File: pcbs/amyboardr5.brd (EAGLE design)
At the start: 106.1 x 47.5 mm, 146 parts, among them Q2 S8050, Q5 S8050, U1 PCM9211PT, U15 H11L1SR2M, U16 SPX3819, U2 ESP32­S2­SOLO, U3 SPX3819, U4 TL074CD, U6 HX3608, Y1 22.5792MHZ

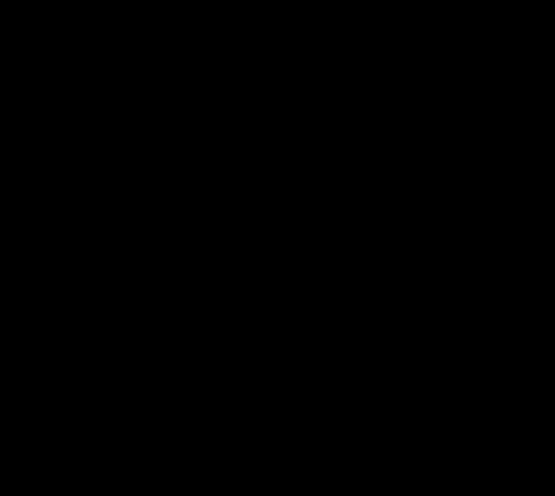
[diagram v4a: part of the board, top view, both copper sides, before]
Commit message: Added ferrite beads in Pi circuits to + and -12v lines.
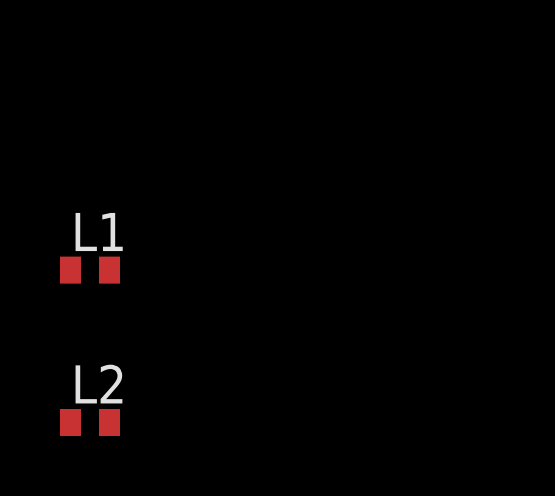
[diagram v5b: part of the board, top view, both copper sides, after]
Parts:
- added L1, L2: BLM15HB121SN1, inductors:0402
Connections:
- new net N$16: C31.2, D10.A, L2.1
- new net N$24: C27.1, D8.C, L1.1
- new net N$25: C29.1
- new net N$30: R18.2
- net -12V: now also L2.2; no longer C31.2, D10.A
- net 12V: now also L1.2; no longer C27.1, C29.1, D8.C, R18.2
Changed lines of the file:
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@@
 <attribute name="VALUE" x="36.83" y="46.99" size="1.27" layer="27" rot="R90"/>
+</element>
+<element name="L1" library="inductors" library_urn="urn:adsk.eagle:library:243" package="0402" package3d_urn="urn:adsk.eagle:package:15132/1" value="BLM15HB121SN1" x="-284.226" y="-1072.388" smashed="yes">
+<attribute name="NAME" x="-284.861" y="-1071.753" size="1.27" layer="25"/>
+<attribute name="POPULARITY" value="0" x="-284.226" y="-1072.388" size="1.778" layer="27" display="off"/>
+<attribute name="VALUE" x="-284.861" y="-1074.293" size="1.27" layer="27"/>
+</element>
+<element name="L2" library="inductors" library_urn="urn:adsk.eagle:library:243" package="0402" package3d_urn="urn:adsk.eagle:package:15132/1" value="BLM15HB121SN1" x="-284.226" y="-1077.468" smashed="yes">
+<attribute name="NAME" x="-284.861" y="-1076.833" size="1.27" layer="25"/>
+<attribute name="POPULARITY" value="0" x="-284.226" y="-1077.468" size="1.778" layer="27" display="off"/>
+<attribute name="VALUE" x="-284.861" y="-1079.373" size="1.27" layer="27"/>
 </element>
 </elements>
@@
 <contactref element="R19" pad="1"/>
 <contactref element="C28" pad="2"/>
-<contactref element="C27" pad="2"/>
 <contactref element="D9" pad="C"/>
 <contactref element="C31" pad="1"/>
@@
 <contactref element="C9" pad="2"/>
 <contactref element="R21" pad="2"/>
+<contactref element="C27" pad="2"/>
 <wire x1="93.69" y1="45.582" x2="95.62" y2="43.652" width="0" layer="19" extent="1-1"/>
 <wire x1="95.62" y1="39.652" x2="95.62" y2="43.652" width="0" layer="19" extent="1-1"/>
@@
 <wire x1="41.148" y1="33.02" x2="36.83" y2="33.02" width="0" layer="19" extent="1-1"/>
 <wire x1="41.656" y1="34.036" x2="41.148" y2="33.02" width="0" layer="19" extent="1-1"/>
+<wire x1="42.418" y1="36.950334375" x2="41.656" y2="34.036" width="0" layer="19" extent="1-1"/>
 <wire x1="53.086" y1="36.950334375" x2="52.782" y2="31.588" width="0" layer="19" extent="1-1"/>
 <wire x1="28.006" y1="14.732" x2="28.448" y2="21.59" width="0" layer="19" extent="1-1"/>
@@
 <wire x1="17.206" y1="2.76" x2="19.606" y2="10.26" width="0" layer="19" extent="1-1"/>
 <wire x1="11.21" y1="3.236" x2="17.206" y2="2.76" width="0" layer="19" extent="1-16"/>
-<wire x1="42.418" y1="36.950334375" x2="37.084" y2="36.83" width="0" layer="19" extent="1-1"/>
 <wire x1="46.331" y1="45.72" x2="42.418" y2="36.950334375" width="0" layer="19" extent="1-1"/>
 <wire x1="45.706" y1="47.27" x2="46.331" y2="45.72" width="0" layer="19" extent="1-1"/>
 <wire x1="50.306" y1="47.27" x2="46.331" y2="45.72" width="0" layer="19" extent="1-1"/>
-<wire x1="34.544" y1="48.752" x2="42.418" y2="36.950334375" width="0" layer="19" extent="1-1"/>
 <wire x1="59.93" y1="47.308" x2="50.306" y2="47.27" width="0" layer="19" extent="1-1"/>
 <wire x1="60.555" y1="45.758" x2="59.93" y2="47.308" width="0" layer="19" extent="1-1"/>
@@
 <wire x1="83.934" y1="42.852" x2="93.69" y2="45.582" width="0" layer="19" extent="1-1"/>
 <wire x1="73.684" y1="35.132" x2="66.434" y2="42.852" width="0" layer="19" extent="1-1"/>
+<wire x1="34.544" y1="48.752" x2="45.706" y2="47.27" width="0" layer="19" extent="1-1"/>
 </signal>
 <signal name="3.3V">
@@
 </signal>
 <signal name="-12V">
-<contactref element="D10" pad="A"/>
-<contactref element="C31" pad="2"/>
 <contactref element="C20" pad="2"/>
 <contactref element="U4" pad="11"/>
 <contactref element="C21" pad="2"/>
-<wire x1="6.858" y1="33.528" x2="3.556" y2="33.528" width="0" layer="19" extent="1-1"/>
-<wire x1="10.16" y1="33.528" x2="6.858" y2="33.528" width="0" layer="19" extent="1-1"/>
-<wire x1="17.519" y1="34.29" x2="10.16" y2="33.528" width="0" layer="19" extent="1-1"/>
-<wire x1="57.593" y1="15.24" x2="17.519" y2="34.29" width="0" layer="19" extent="1-1"/>
+<contactref element="L2" pad="2"/>
+<wire x1="57.593" y1="15.24" x2="-283.576" y2="-1077.468" width="0" layer="19" extent="1-1"/>
+<wire x1="6.858" y1="33.528" x2="57.593" y2="15.24" width="0" layer="19" extent="1-1"/>
+<wire x1="3.556" y1="33.528" x2="6.858" y2="33.528" width="0" layer="19" extent="1-1"/>
 </signal>
 <signal name="+12V">
@@
 </signal>
 <signal name="12V">
-<contactref element="C28" pad="1"/>
-<contactref element="C27" pad="1"/>
-<contactref element="D8" pad="C"/>
-<contactref element="C29" pad="1"/>
 <contactref element="R17" pad="2"/>
-<contactref element="R18" pad="2"/>
 <contactref element="C32" pad="1"/>
 <contactref element="U3" pad="1"/>
 <contactref element="U3" pad="3"/>
-<wire x1="33.274" y1="38.1" x2="36.576" y2="38.1" width="0" layer="19" extent="1-1"/>
-<wire x1="29.972" y1="38.1" x2="33.274" y2="38.1" width="0" layer="19" extent="1-1"/>
-<wire x1="35.56" y1="34.036" x2="36.576" y2="38.1" width="0" layer="19" extent="1-1"/>
-<wire x1="39.37" y1="34.036" x2="35.56" y2="34.036" width="0" layer="19" extent="1-1"/>
+<contactref element="C28" pad="1"/>
+<contactref element="L1" pad="2"/>
+<wire x1="35.56" y1="34.036" x2="-283.576" y2="-1072.388" width="0" layer="19" extent="1-1"/>
 <wire x1="35.306" y1="27.94" x2="35.56" y2="34.036" width="0" layer="19" extent="1-1"/>
+<wire x1="29.972" y1="38.1" x2="35.56" y2="34.036" width="0" layer="19" extent="1-1"/>
 <wire x1="36.134" y1="21.0519" x2="35.306" y2="27.94" width="0" layer="19" extent="1-1"/>
 <wire x1="38.034" y1="21.0519" x2="36.134" y2="21.0519" width="0" layer="19" extent="1-1"/>
-<wire x1="38.107" y1="20.574" x2="38.034" y2="21.0519" width="0" layer="19" extent="1-1"/>
 </signal>
 <signal name="N$29">
@@
 <wire x1="34.544" y1="36.592" x2="46.908046875" y2="40.64" width="0" layer="19" extent="1-1"/>
 </signal>
+<signal name="N$16">
+<contactref element="D10" pad="A"/>
+<contactref element="C31" pad="2"/>
+<contactref element="L2" pad="1"/>
+<wire x1="17.519" y1="34.29" x2="-284.876" y2="-1077.468" width="0" layer="19" extent="1-1"/>
+<wire x1="10.16" y1="33.528" x2="17.519" y2="34.29" width="0" layer="19" extent="1-1"/>
+</signal>
+<signal name="N$24">
+<contactref element="C27" pad="1"/>
+<contactref element="L1" pad="1"/>
+<contactref element="D8" pad="C"/>
+<wire x1="33.274" y1="38.1" x2="-284.876" y2="-1072.388" width="0" layer="19" extent="1-1"/>
+<wire x1="38.107" y1="20.574" x2="33.274" y2="38.1" width="0" layer="19" extent="1-1"/>
+</signal>
+<signal name="N$25">
+<contactref element="C29" pad="1"/>
+</signal>
+<signal name="N$30">
+<contactref element="R18" pad="2"/>
+</signal>
 </signals>

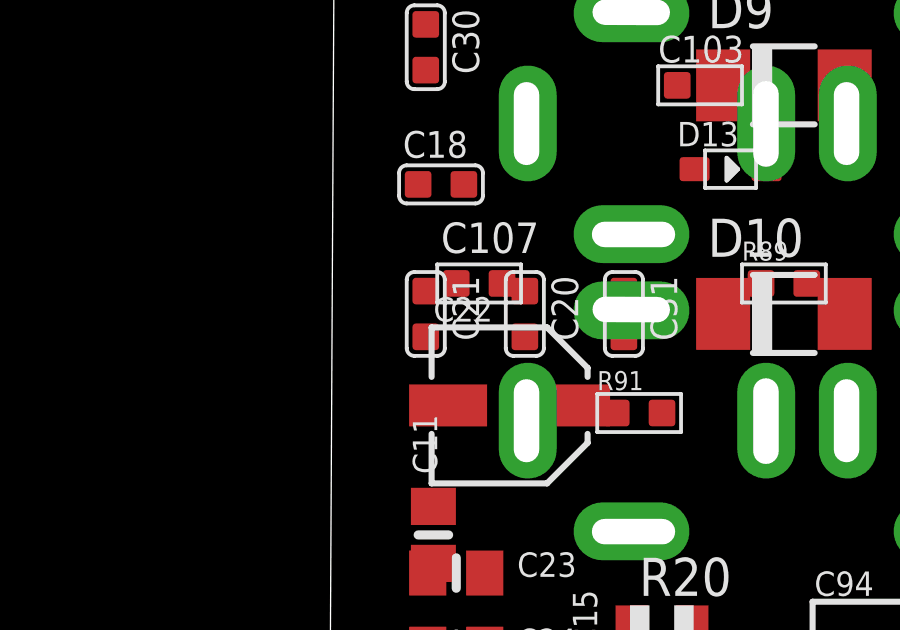
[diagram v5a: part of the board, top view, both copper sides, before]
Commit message: Moved GP8413 and 5V LDO to +12V_UNFILTERED.
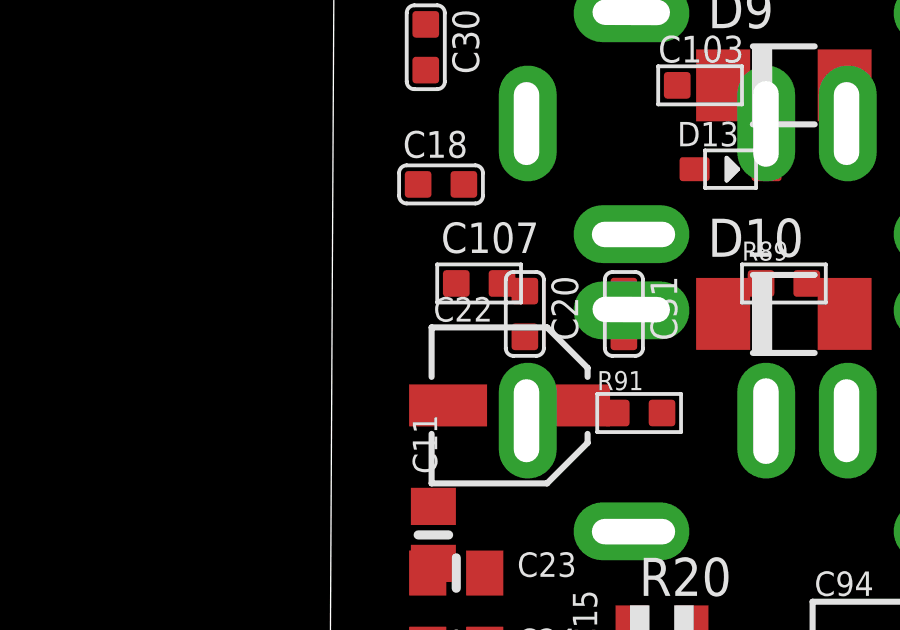
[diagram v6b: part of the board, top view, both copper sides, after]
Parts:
- removed C21: 20pF, Discrete-new:C0603
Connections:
- removed net N$24: C27.1, D8.C, L1.1
- new net 12V_UNFILTERED: C26.1, C27.1, C32.1, D8.C, L1.1, U$7.5, U3.1, U3.3
- net +12V: no longer C21.1, C26.1, U$7.5
- net -12V: no longer C21.2
- net 12V: no longer C32.1, U3.1, U3.3
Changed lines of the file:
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@@
 <attribute name="VALUE" x="6.9215" y="34.29" size="0.635" layer="27" ratio="10" rot="R270" align="center"/>
-</element>
-<element name="C21" library="Discrete-new" package="C0603" value="20pF" x="3.556" y="34.29" smashed="yes">
-<attribute name="NAME" x="4.445" y="35.56" size="0.889" layer="25" ratio="11" rot="R270"/>
-<attribute name="NAME" x="3.302" y="35.56" size="0.635" layer="33" ratio="10" rot="R270"/>
-<attribute name="VALUE" x="3.6195" y="34.29" size="0.635" layer="27" ratio="10" rot="R270" align="center"/>
 </element>
 <element name="R20" library="adafruit" package="R0805" value="10K" x="11.43" y="23.876" smashed="yes">
@@
 <contactref element="C20" pad="2"/>
 <contactref element="U4" pad="11"/>
-<contactref element="C21" pad="2"/>
 <contactref element="L2" pad="2"/>
 <wire x1="57.593" y1="15.24" x2="-283.576" y2="-1077.468" width="0" layer="19" extent="1-1"/>
 <wire x1="6.858" y1="33.528" x2="57.593" y2="15.24" width="0" layer="19" extent="1-1"/>
-<wire x1="3.556" y1="33.528" x2="6.858" y2="33.528" width="0" layer="19" extent="1-1"/>
 </signal>
 <signal name="+12V">
 <contactref element="U4" pad="4"/>
-<contactref element="C21" pad="1"/>
-<contactref element="U$7" pad="5"/>
-<contactref element="C26" pad="1"/>
-<wire x1="3.556" y1="35.052" x2="3.622" y2="20.574" width="0" layer="19" extent="1-1"/>
-<wire x1="52.643" y1="15.24" x2="3.556" y2="35.052" width="0" layer="19" extent="1-1"/>
-<wire x1="51.054" y1="24.07" x2="52.643" y2="15.24" width="0" layer="19" extent="1-1"/>
 </signal>
 <signal name="GND3">
@@
 <signal name="12V">
 <contactref element="R17" pad="2"/>
-<contactref element="C32" pad="1"/>
-<contactref element="U3" pad="1"/>
-<contactref element="U3" pad="3"/>
 <contactref element="C28" pad="1"/>
 <contactref element="L1" pad="2"/>
 <wire x1="35.56" y1="34.036" x2="-283.576" y2="-1072.388" width="0" layer="19" extent="1-1"/>
-<wire x1="35.306" y1="27.94" x2="35.56" y2="34.036" width="0" layer="19" extent="1-1"/>
 <wire x1="29.972" y1="38.1" x2="35.56" y2="34.036" width="0" layer="19" extent="1-1"/>
-<wire x1="36.134" y1="21.0519" x2="35.306" y2="27.94" width="0" layer="19" extent="1-1"/>
-<wire x1="38.034" y1="21.0519" x2="36.134" y2="21.0519" width="0" layer="19" extent="1-1"/>
 </signal>
 <signal name="N$29">
@@
 <wire x1="10.16" y1="33.528" x2="17.519" y2="34.29" width="0" layer="19" extent="1-1"/>
 </signal>
-<signal name="N$24">
+<signal name="12V_UNFILTERED">
 <contactref element="C27" pad="1"/>
 <contactref element="L1" pad="1"/>
 <contactref element="D8" pad="C"/>
-<wire x1="33.274" y1="38.1" x2="-284.876" y2="-1072.388" width="0" layer="19" extent="1-1"/>
-<wire x1="38.107" y1="20.574" x2="33.274" y2="38.1" width="0" layer="19" extent="1-1"/>
+<contactref element="U3" pad="1"/>
+<contactref element="C32" pad="1"/>
+<contactref element="U3" pad="3"/>
+<contactref element="U$7" pad="5"/>
+<contactref element="C26" pad="1"/>
+<wire x1="51.054" y1="24.07" x2="-284.876" y2="-1072.388" width="0" layer="19" extent="1-1"/>
+<wire x1="38.034" y1="21.0519" x2="51.054" y2="24.07" width="0" layer="19" extent="1-1"/>
+<wire x1="38.107" y1="20.574" x2="38.034" y2="21.0519" width="0" layer="19" extent="1-1"/>
+<wire x1="36.134" y1="21.0519" x2="38.034" y2="21.0519" width="0" layer="19" extent="1-1"/>
+<wire x1="35.306" y1="27.94" x2="36.134" y2="21.0519" width="0" layer="19" extent="1-1"/>
+<wire x1="33.274" y1="38.1" x2="35.306" y2="27.94" width="0" layer="19" extent="1-1"/>
+<wire x1="3.622" y1="20.574" x2="36.134" y2="21.0519" width="0" layer="19" extent="1-1"/>
 </signal>
 <signal name="N$25">

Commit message: copying usb fb
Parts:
- removed L1, L2: BLM15HB121SN1, inductors:0402
- added FB1, FB2: 100Mhz@120R, rcl:R0805
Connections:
- net -12V: now also FB1.2; no longer L2.2
- net 12V: now also FB2.2; no longer L1.2
- net 12V_UNFILTERED: now also FB2.1; no longer L1.1
- net N$16: now also FB1.1; no longer L2.1
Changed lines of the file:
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@@
 <attribute name="VALUE" x="36.83" y="46.99" size="1.27" layer="27" rot="R90"/>
 </element>
-<element name="L1" library="inductors" library_urn="urn:adsk.eagle:library:243" package="0402" package3d_urn="urn:adsk.eagle:package:15132/1" value="BLM15HB121SN1" x="-284.226" y="-1072.388" smashed="yes">
-<attribute name="NAME" x="-284.861" y="-1071.753" size="1.27" layer="25"/>
-<attribute name="POPULARITY" value="0" x="-284.226" y="-1072.388" size="1.778" layer="27" display="off"/>
-<attribute name="VALUE" x="-284.861" y="-1074.293" size="1.27" layer="27"/>
+<element name="FB1" library="rcl" package="R0805" value="100Mhz@120R" x="-283.718" y="-1083.056" smashed="yes">
+<attribute name="NAME" x="-284.353" y="-1081.786" size="1.27" layer="25"/>
+<attribute name="VALUE" x="-284.353" y="-1085.596" size="1.27" layer="27"/>
 </element>
-<element name="L2" library="inductors" library_urn="urn:adsk.eagle:library:243" package="0402" package3d_urn="urn:adsk.eagle:package:15132/1" value="BLM15HB121SN1" x="-284.226" y="-1077.468" smashed="yes">
-<attribute name="NAME" x="-284.861" y="-1076.833" size="1.27" layer="25"/>
-<attribute name="POPULARITY" value="0" x="-284.226" y="-1077.468" size="1.778" layer="27" display="off"/>
-<attribute name="VALUE" x="-284.861" y="-1079.373" size="1.27" layer="27"/>
+<element name="FB2" library="rcl" package="R0805" value="100Mhz@120R" x="-283.718" y="-1089.406" smashed="yes">
+<attribute name="NAME" x="-284.353" y="-1088.136" size="1.27" layer="25"/>
+<attribute name="VALUE" x="-284.353" y="-1091.946" size="1.27" layer="27"/>
 </element>
 </elements>
@@
 <contactref element="C20" pad="2"/>
 <contactref element="U4" pad="11"/>
-<contactref element="L2" pad="2"/>
-<wire x1="57.593" y1="15.24" x2="-283.576" y2="-1077.468" width="0" layer="19" extent="1-1"/>
+<contactref element="FB1" pad="2"/>
+<wire x1="57.593" y1="15.24" x2="-282.768" y2="-1083.056" width="0" layer="19" extent="1-1"/>
 <wire x1="6.858" y1="33.528" x2="57.593" y2="15.24" width="0" layer="19" extent="1-1"/>
 </signal>
@@
 <contactref element="R17" pad="2"/>
 <contactref element="C28" pad="1"/>
-<contactref element="L1" pad="2"/>
-<wire x1="35.56" y1="34.036" x2="-283.576" y2="-1072.388" width="0" layer="19" extent="1-1"/>
+<contactref element="FB2" pad="2"/>
+<wire x1="35.56" y1="34.036" x2="-282.768" y2="-1089.406" width="0" layer="19" extent="1-1"/>
 <wire x1="29.972" y1="38.1" x2="35.56" y2="34.036" width="0" layer="19" extent="1-1"/>
 </signal>
@@
 <contactref element="D10" pad="A"/>
 <contactref element="C31" pad="2"/>
-<contactref element="L2" pad="1"/>
-<wire x1="17.519" y1="34.29" x2="-284.876" y2="-1077.468" width="0" layer="19" extent="1-1"/>
+<contactref element="FB1" pad="1"/>
+<wire x1="17.519" y1="34.29" x2="-284.668" y2="-1083.056" width="0" layer="19" extent="1-1"/>
 <wire x1="10.16" y1="33.528" x2="17.519" y2="34.29" width="0" layer="19" extent="1-1"/>
 </signal>
 <signal name="12V_UNFILTERED">
 <contactref element="C27" pad="1"/>
-<contactref element="L1" pad="1"/>
 <contactref element="D8" pad="C"/>
 <contactref element="U3" pad="1"/>
@@
 <contactref element="U$7" pad="5"/>
 <contactref element="C26" pad="1"/>
-<wire x1="51.054" y1="24.07" x2="-284.876" y2="-1072.388" width="0" layer="19" extent="1-1"/>
+<contactref element="FB2" pad="1"/>
+<wire x1="51.054" y1="24.07" x2="-284.668" y2="-1089.406" width="0" layer="19" extent="1-1"/>
 <wire x1="38.034" y1="21.0519" x2="51.054" y2="24.07" width="0" layer="19" extent="1-1"/>
 <wire x1="38.107" y1="20.574" x2="38.034" y2="21.0519" width="0" layer="19" extent="1-1"/>
